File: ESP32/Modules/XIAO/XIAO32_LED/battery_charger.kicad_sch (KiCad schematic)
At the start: 8 parts, among them U2 TPS61023DRLR

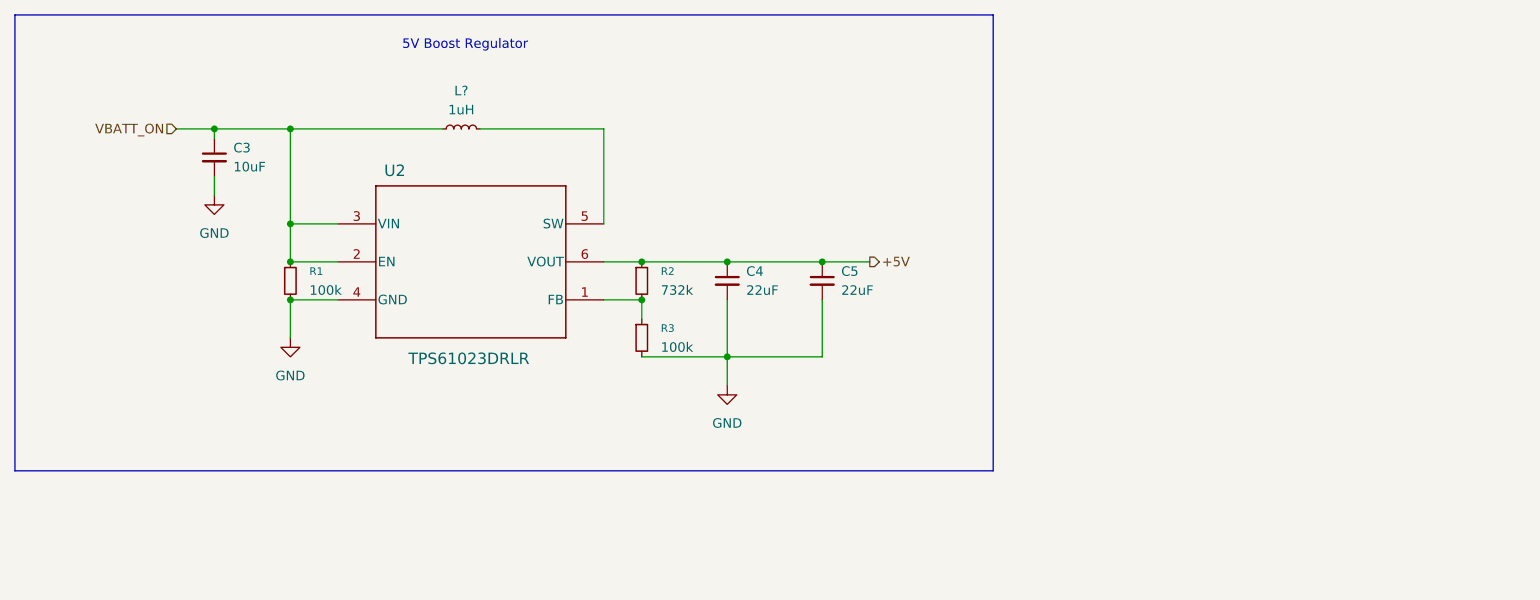
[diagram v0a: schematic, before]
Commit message: XIAO32_LED: Convert sch to hierarchical pins
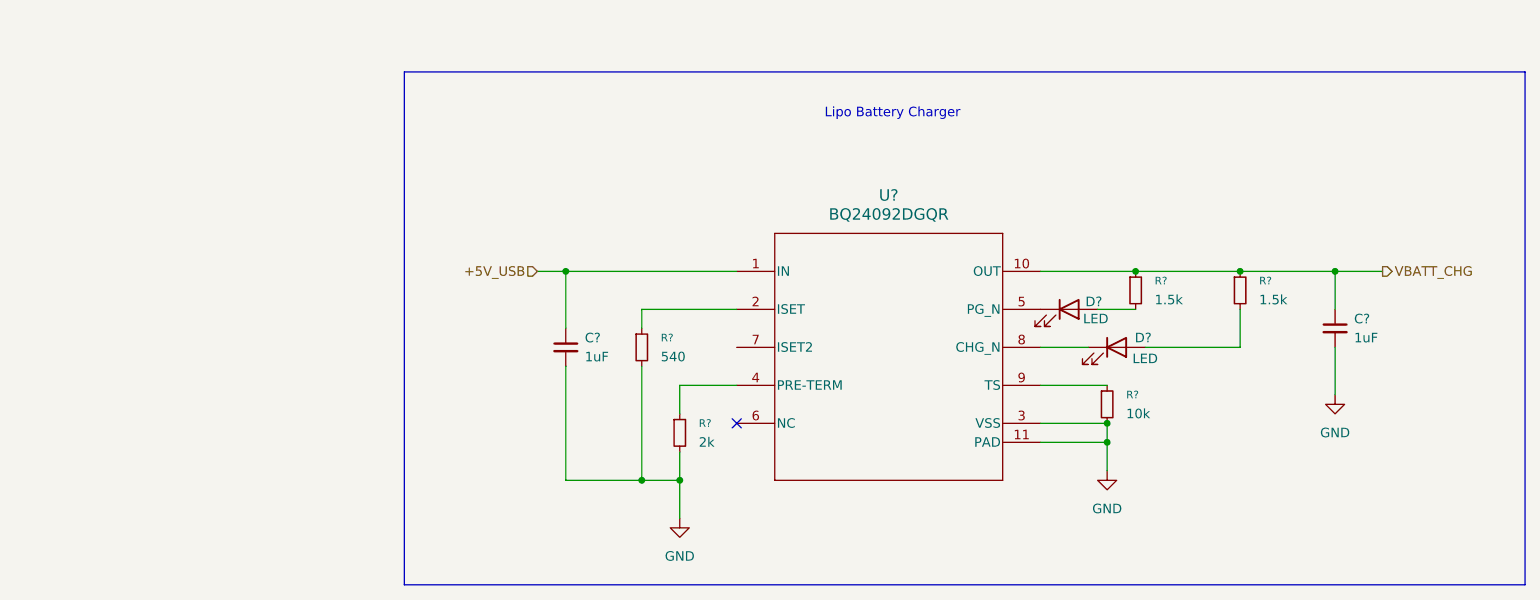
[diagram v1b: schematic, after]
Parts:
- removed C3: 10uF, symbol Device:C_Small
- removed C4, C5: 22uF, symbol Device:C_Small
- removed L?: 1uH, symbol Device:L_Small
- removed R1, R3: 100k, symbol Device:R_Small
- removed R2: 732k, symbol Device:R_Small
- removed U2: TPS61023DRLR, DRL0006A, symbol My_Converter_DCDC:TPS61023DRLR
- added C? (x2): 1uF, symbol Device:C_Small
- added D? (x2): LED, symbol Device:LED
- added R? (x2): 1.5k, symbol Device:R_Small
- added R?: 540, symbol Device:R_Small
- added R?: 2k, symbol Device:R_Small
- added R?: 10k, symbol Device:R_Small
- added U?: BQ24092DGQR, Package_SO:MSOP-10-1EP_3x3mm_P0.5mm_EP1.73x1.98mm, symbol My_Battery_Management:BQ24092DGQR
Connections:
- net GND: now also C?.2, C?.2, R?.2, R?.2, R?.2, U?.11 (PAD), U?.3 (VSS)
- new net: D?.2 (A), R?.2 (x2)
- new net: R?.1, U?.2 (ISET)
- new net: R?.1, U?.4 (PRE-TERM)
- new net: D?.1 (K), U?.5 (PG_N)
- new net: D?.1 (K), U?.8 (CHG_N)
- new net: R?.1, U?.9 (TS)
- new net +5V_USB: C?.1, U?.1 (IN)
- new net VBATT_CHG: C?.1, R?.1, R?.1, U?.10 (OUT)
- no-connect marks 0 -> 1
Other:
- note added: "Lipo Battery Charger"
- note removed: "5V Boost Regulator"
